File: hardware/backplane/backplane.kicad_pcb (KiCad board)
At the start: 2 copper layers, 199 x 123 mm, 81 parts, among them J1 C96ABC, J10 Conn_Coaxial_Power, J2 C96ABC, J3 C96ABC, J4 C96ABC, J5 C96ABC, J6 C96ABC, J7 C96ABC, J8 C96ABC, J9 C96ABC, SW1 SW_Push, SW2 SW_SPDT, SW3 SW_SPDT, U1 74AHC14, U10 U13, U2 74AHC08, U4 74HC00, U7 NE556, U9 74AHCT125, X1 CXO_DIP8

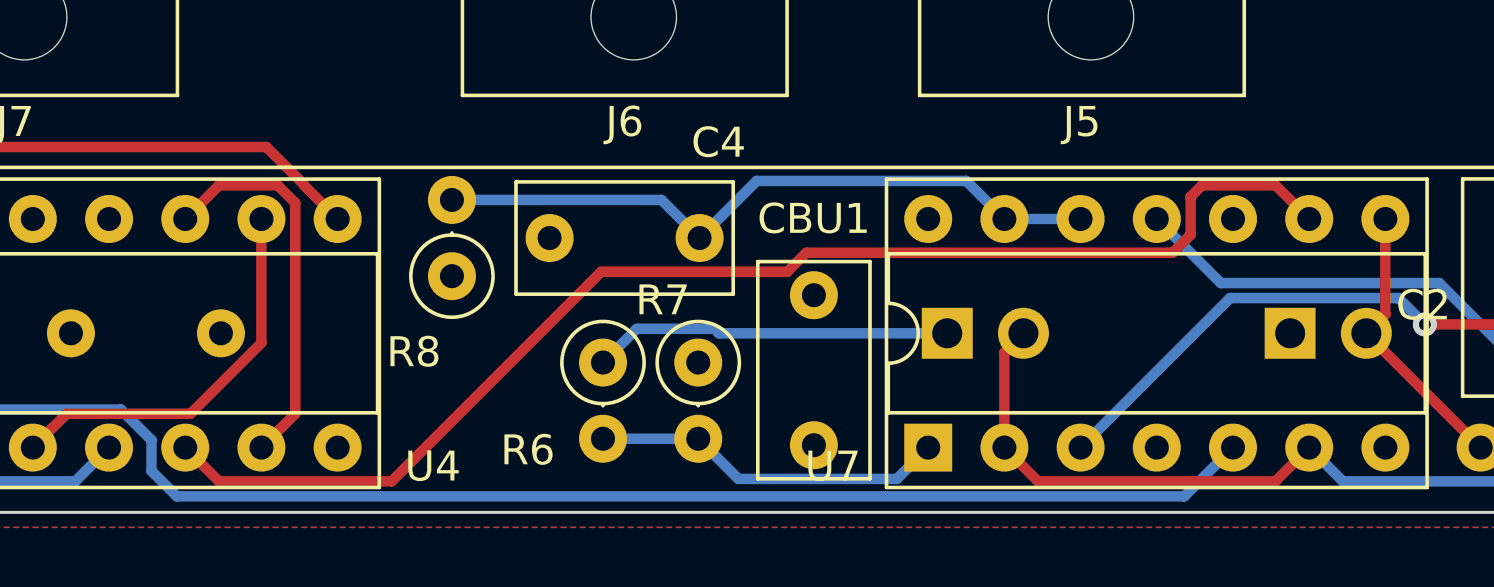
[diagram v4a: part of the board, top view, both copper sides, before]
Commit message: backplane: move a track
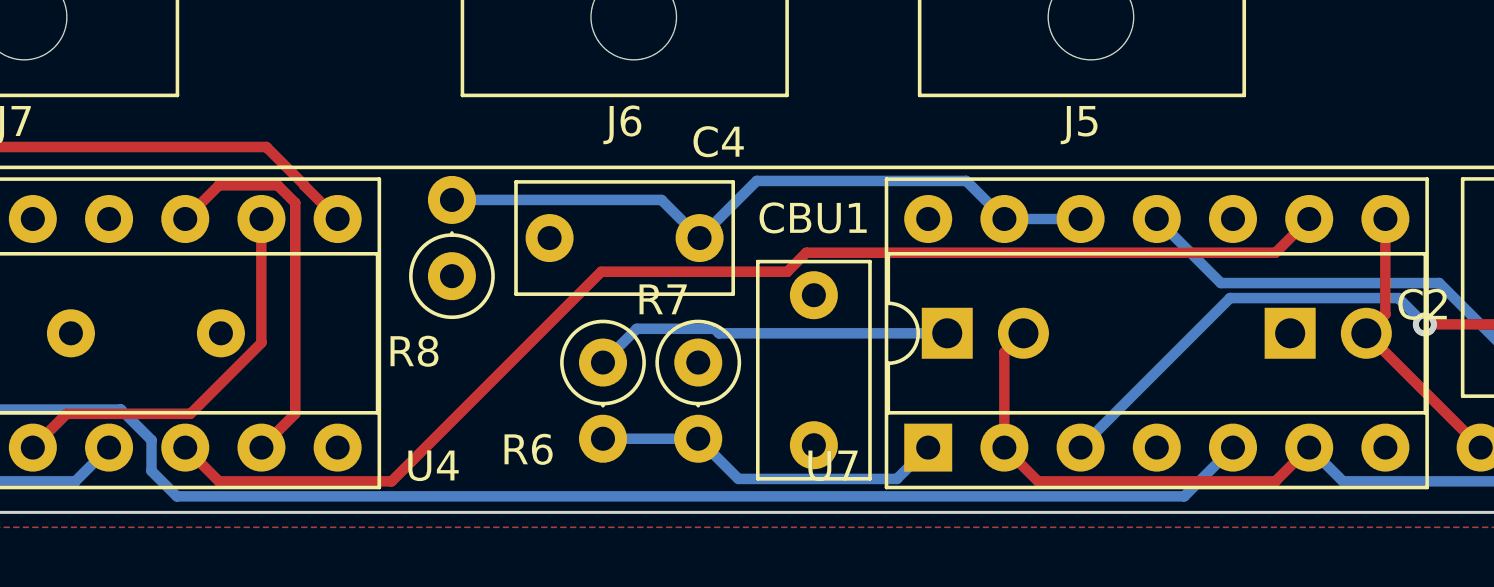
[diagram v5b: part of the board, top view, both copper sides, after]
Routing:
- net 555_MONO: track 43.2 -> 41.6 mm
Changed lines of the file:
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@@
     (thickness 1.6)
     (drawings 478)
-    (tracks 2376)
+    (tracks 2372)
     (zones 0)
     (modules 81)
@@
   (segment (start 118.02 141.605) (end 125.005 141.605) (width 0.35) (layer B.Cu) (net 343))
   (segment (start 136.435 142.24) (end 138.975 142.24) (width 0.35) (layer B.Cu) (net 343))
-  (segment (start 110.255001 150.985001) (end 116.009999 150.985001) (width 0.35) (layer F.Cu) (net 344))
-  (segment (start 109.13 149.86) (end 110.255001 150.985001) (width 0.35) (layer F.Cu) (net 344))
-  (segment (start 129.199997 144.000001) (end 129.834997 143.365001) (width 0.35) (layer F.Cu) (net 344))
-  (segment (start 122.994999 144.000001) (end 129.199997 144.000001) (width 0.35) (layer F.Cu) (net 344))
-  (segment (start 116.009999 150.985001) (end 122.994999 144.000001) (width 0.35) (layer F.Cu) (net 344))
-  (segment (start 145.469999 141.114999) (end 143.025001 141.114999) (width 0.35) (layer F.Cu) (net 344))
-  (segment (start 146.595 142.24) (end 145.469999 141.114999) (width 0.35) (layer F.Cu) (net 344))
-  (segment (start 142.640001 142.769999) (end 142.044999 143.365001) (width 0.35) (layer F.Cu) (net 344))
-  (segment (start 142.640001 141.499999) (end 142.640001 142.769999) (width 0.35) (layer F.Cu) (net 344))
-  (segment (start 143.025001 141.114999) (end 142.640001 141.499999) (width 0.35) (layer F.Cu) (net 344))
-  (segment (start 129.834997 143.365001) (end 142.044999 143.365001) (width 0.35) (layer F.Cu) (net 344))
+  (segment (start 110.255001 150.985001) (end 109.13 149.86) (width 0.35) (layer F.Cu) (net 344))
+  (segment (start 116.009999 150.985001) (end 110.255001 150.985001) (width 0.35) (layer F.Cu) (net 344))
+  (segment (start 122.994999 144.000001) (end 116.009999 150.985001) (width 0.35) (layer F.Cu) (net 344))
+  (segment (start 129.199997 144.000001) (end 122.994999 144.000001) (width 0.35) (layer F.Cu) (net 344))
+  (segment (start 129.834997 143.365001) (end 129.199997 144.000001) (width 0.35) (layer F.Cu) (net 344))
+  (segment (start 145.469999 143.365001) (end 129.834997 143.365001) (width 0.35) (layer F.Cu) (net 344))
+  (segment (start 146.595 142.24) (end 145.469999 143.365001) (width 0.35) (layer F.Cu) (net 344))
   (segment (start 149.135 145.415) (end 148.5 146.05) (width 0.35) (layer F.Cu) (net 356))
   (segment (start 149.135 142.24) (end 149.135 145.415) (width 0.35) (layer F.Cu) (net 356))

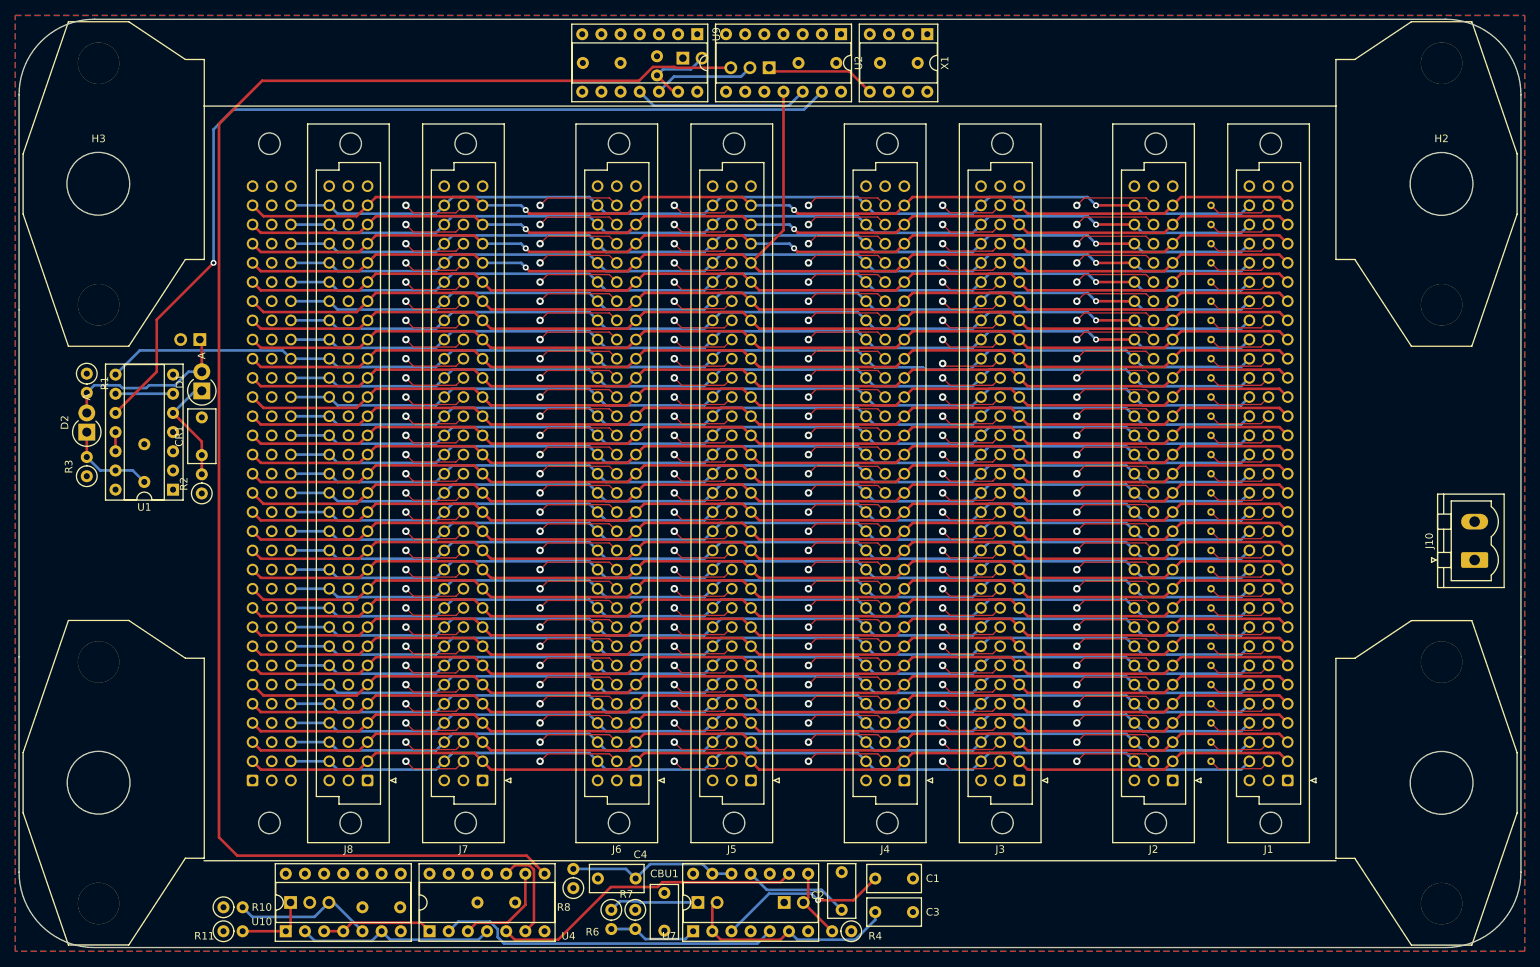
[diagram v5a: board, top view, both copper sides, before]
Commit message: backplane: bump some clearance hole diameters
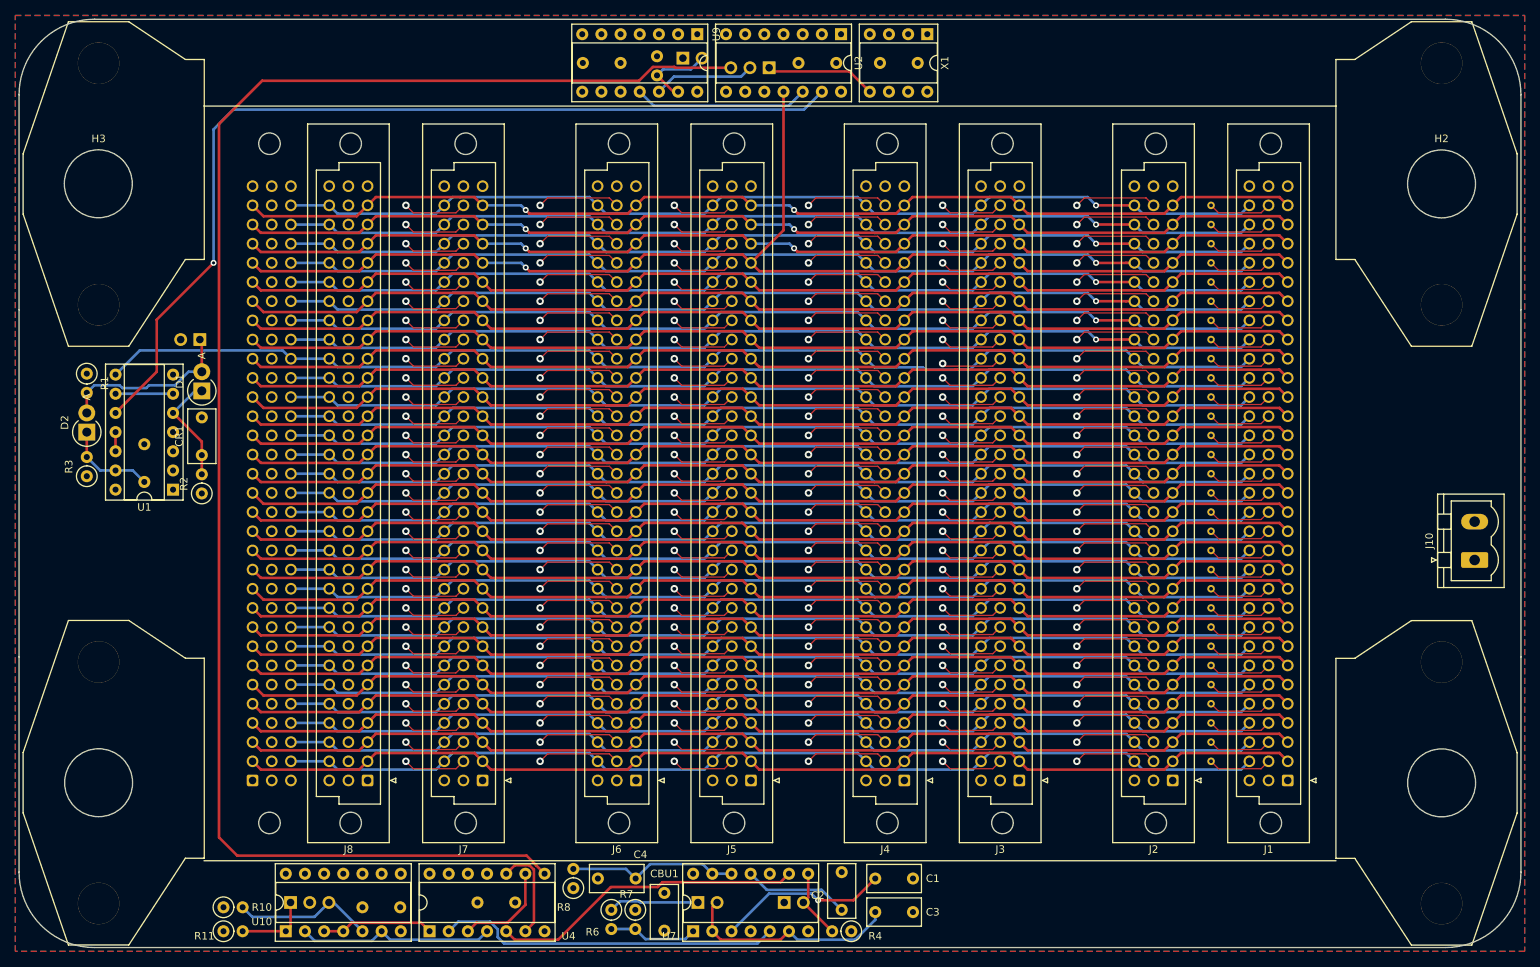
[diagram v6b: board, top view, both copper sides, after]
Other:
- outline, holes or cut-outs redrawn

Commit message: backplane: use less mounting hardware
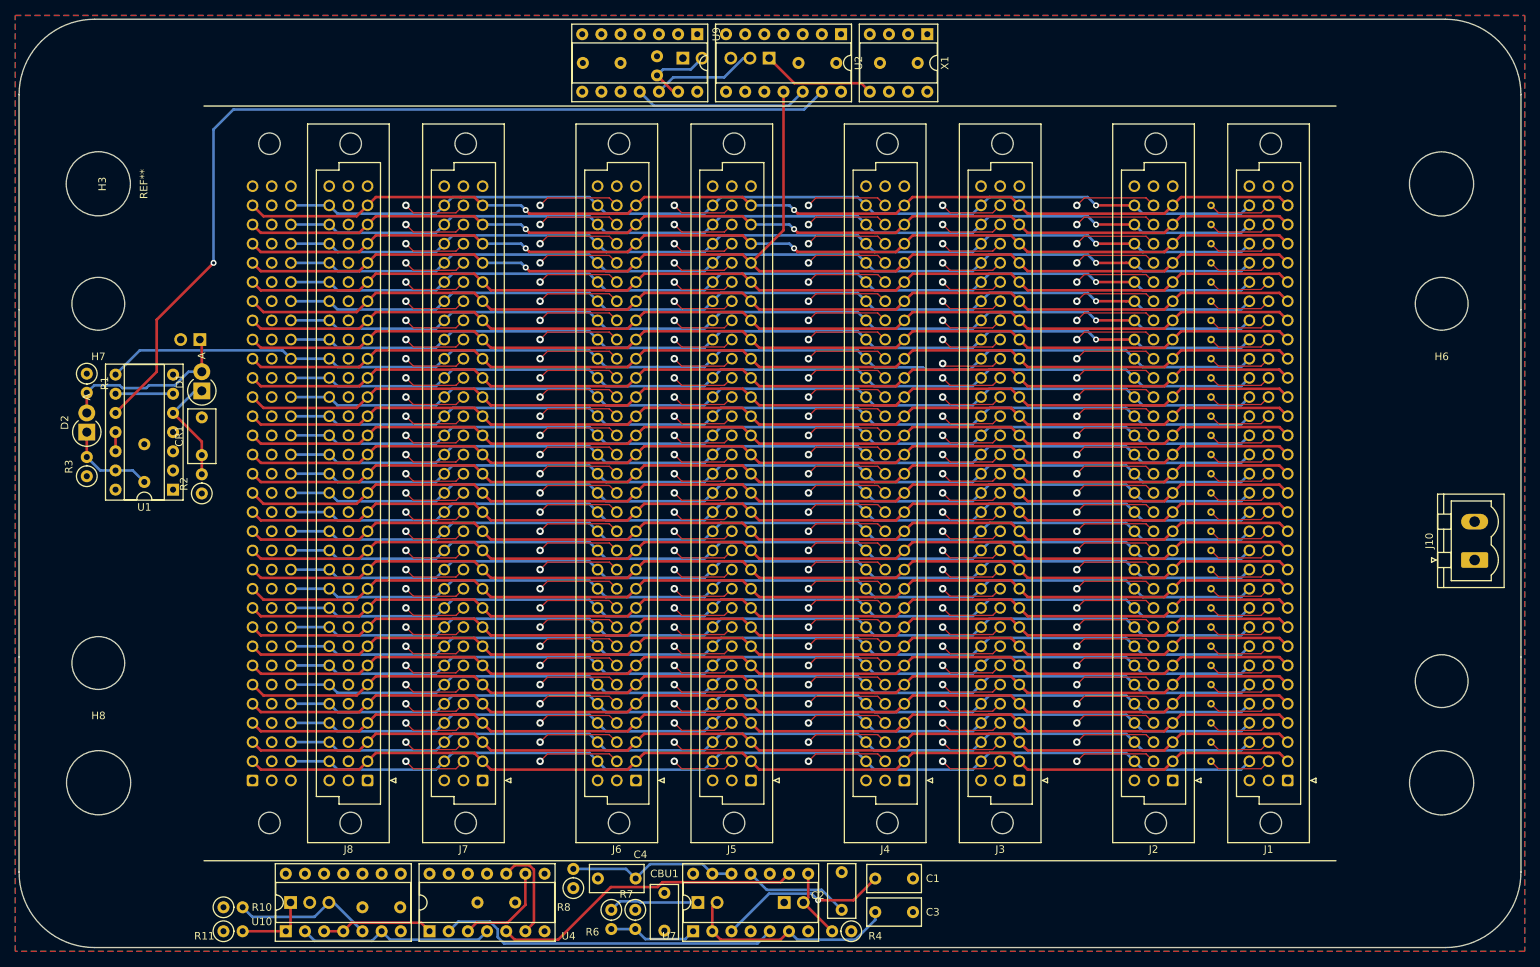
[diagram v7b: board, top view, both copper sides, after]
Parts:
- added H5: MountingHole, rails:7mm, B.Cu at (233.1, 116.7)
- added H6: MountingHole, rails:7mm, F.Cu at (233.1, 66.7)
- added H7: MountingHole, rails:7mm, F.Cu at (55.1, 66.7)
- added H8: MountingHole, rails:7mm, F.Cu at (55.1, 114.3)
- H1, H3, H4: footprint rails:SHF8-L -> rails:8mm
- H2: footprint rails:SHF8-R -> rails:8mm; moved to B.Cu
- moved SW2 1.27 mm to (144.0, 34.2)
- turned H2 to 90 degrees
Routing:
- net 555_CLK: track 210.7 -> 0.00 mm
- net XO: track 14.7 -> 15.2 mm
- net Net-(SW2-Pad2): track 13.4 -> 13.9 mm
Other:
- outline, holes or cut-outs redrawn

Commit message: backplane: 4 screw bars to 2
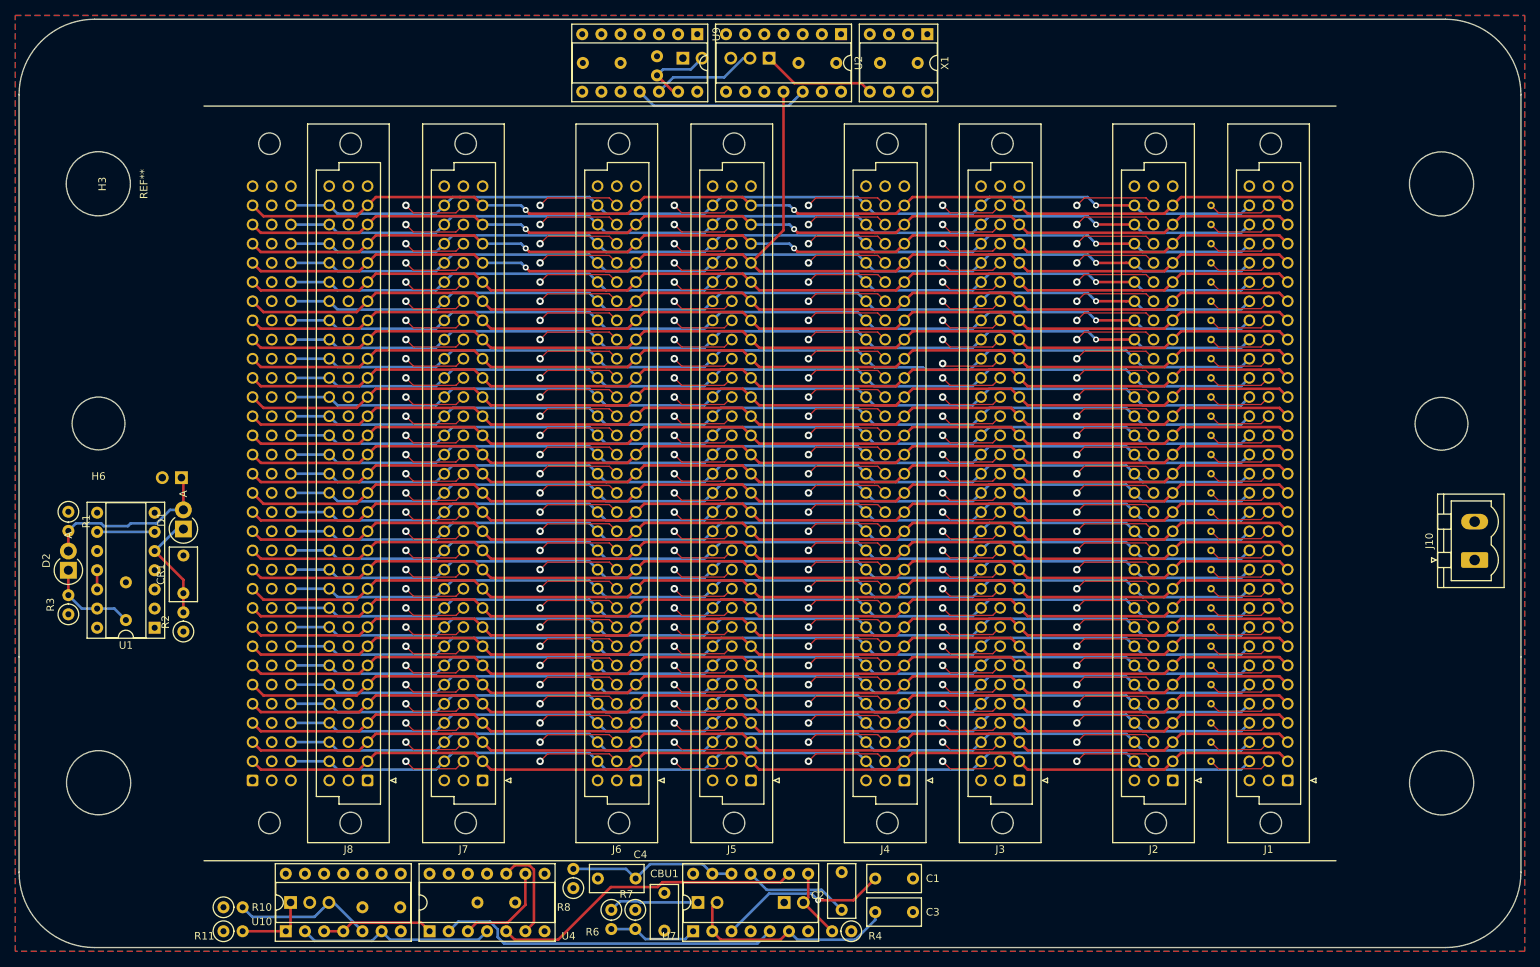
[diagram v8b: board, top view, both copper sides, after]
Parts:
- removed H7, H8: MountingHole, rails:7mm
- moved H6 178.7 mm to (55.1, 82.6)
- moved H5 34.1 mm to (233.1, 82.6)
- moved CR2 18.5 mm to (58.7, 108.6)
- moved D2 18.5 mm to (51.1, 102.0)
- moved JPC1 18.5 mm to (66.1, 89.8)
- moved R1 18.5 mm to (51.1, 94.3)
- moved R2 18.5 mm to (66.4, 110.2)
- moved R3 18.5 mm to (51.1, 107.9)
- moved CR1 18.5 mm to (66.4, 105.1)
- moved D1 18.5 mm to (66.4, 96.6)
- moved U1 18.5 mm to (62.5, 109.6)
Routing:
- net ~CLK_RST~: track 125.6 -> 0.00 mm, vias 1 -> 0
- net C23: track 158.7 -> 133.7 mm
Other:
- outline, holes or cut-outs redrawn
